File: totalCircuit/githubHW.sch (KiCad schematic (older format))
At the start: 410 parts, among them J1 Conn_01x06, J2 Conn_01x07, J3 Conn_01x07, J4 Conn_01x07, J5 Conn_01x07, J6 Conn_01x06, SW1 SW_Push, SW2 SW_Push, SW3 SW_Push, SW4 SW_Push, U1 WeMos_mini, U2 TPIC6B595N, U3 TLC5940NT, U4 TPIC6B595N

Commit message: documentation updated
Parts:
- gave numbers to parts that had none: 268

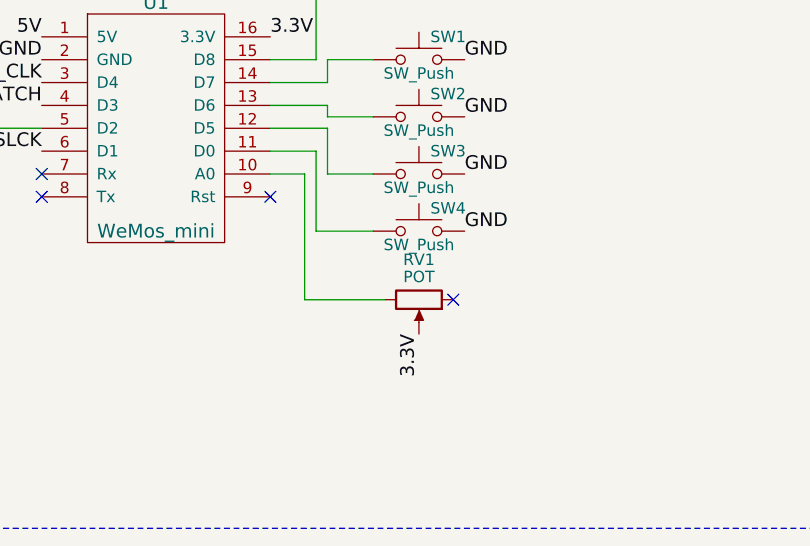
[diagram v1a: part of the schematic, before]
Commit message: poti connection corrected
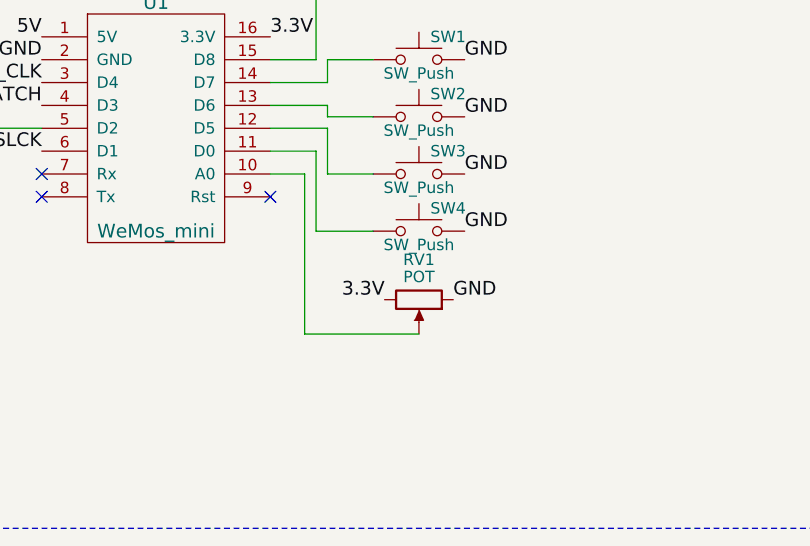
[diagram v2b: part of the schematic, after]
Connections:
- net 3.3V: now also RV1.3; no longer RV1.2
- net GND: now also RV1.1
- net at U1.10 (A0): now also RV1.2; no longer RV1.3
- no-connect marks 10 -> 9
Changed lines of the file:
@@
 	0    1    1    0
 $EndComp
-NoConn ~ 3600 10300
 $Comp
 L TPIC6B595N U2
@@
 	-1   0    0    -1
 $EndComp
-Text Label 3450 10450 3    60   ~ 0
+Text Label 3300 10300 2    60   ~ 0
 3.3V
 Text Label 2800 9150 0    60   ~ 0
@@
 	2950 9750 2800 9750
 Wire Wire Line
-	2950 10300 2950 9750
-Wire Wire Line
-	3300 10300 2950 10300
+	2950 9750 2950 10450
 Wire Wire Line
 	3000 10000 3250 10000
@@
 Wire Notes Line
 	25950 9150 25950 1200
+Text Label 3600 10300 0    60   ~ 0
+GND
+Wire Wire Line
+	2950 10450 3450 10450
 $EndSCHEMATC
